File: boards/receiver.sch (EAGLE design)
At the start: 86 parts, among them IC1 7805DT, IC3 XMEGA128a3u, Q1 BC846BSMD, Q2 BC846BSMD, Q3 BC846BSMD, Q4 BC846BSMD, Q5 BC846BSMD, Q6 BC846BSMD, Q7 BC846BSMD, Q8 BC846BSMD

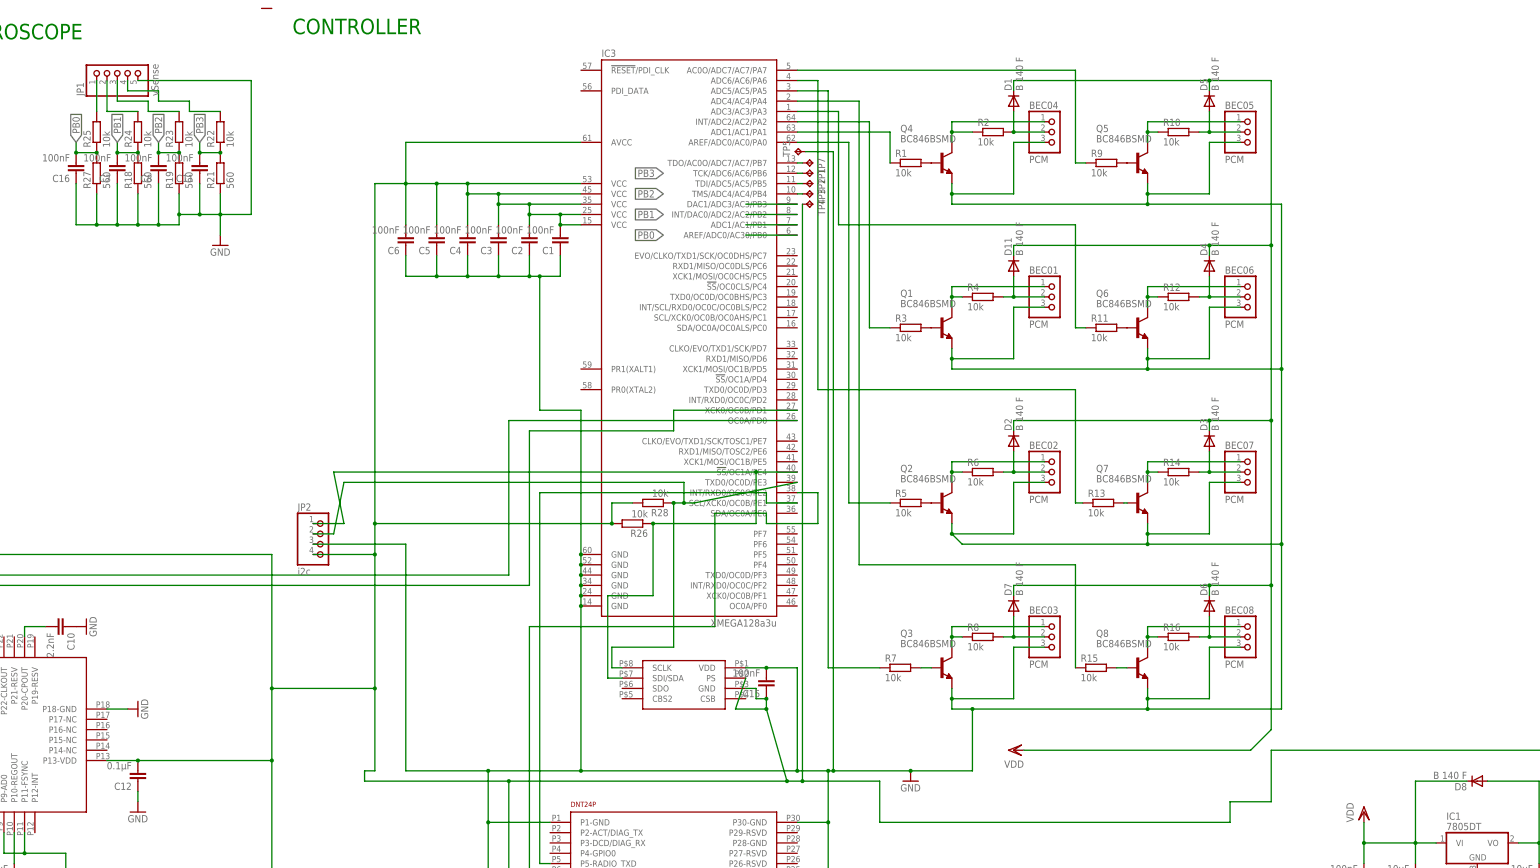
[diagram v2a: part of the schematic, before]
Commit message: Added some status leds
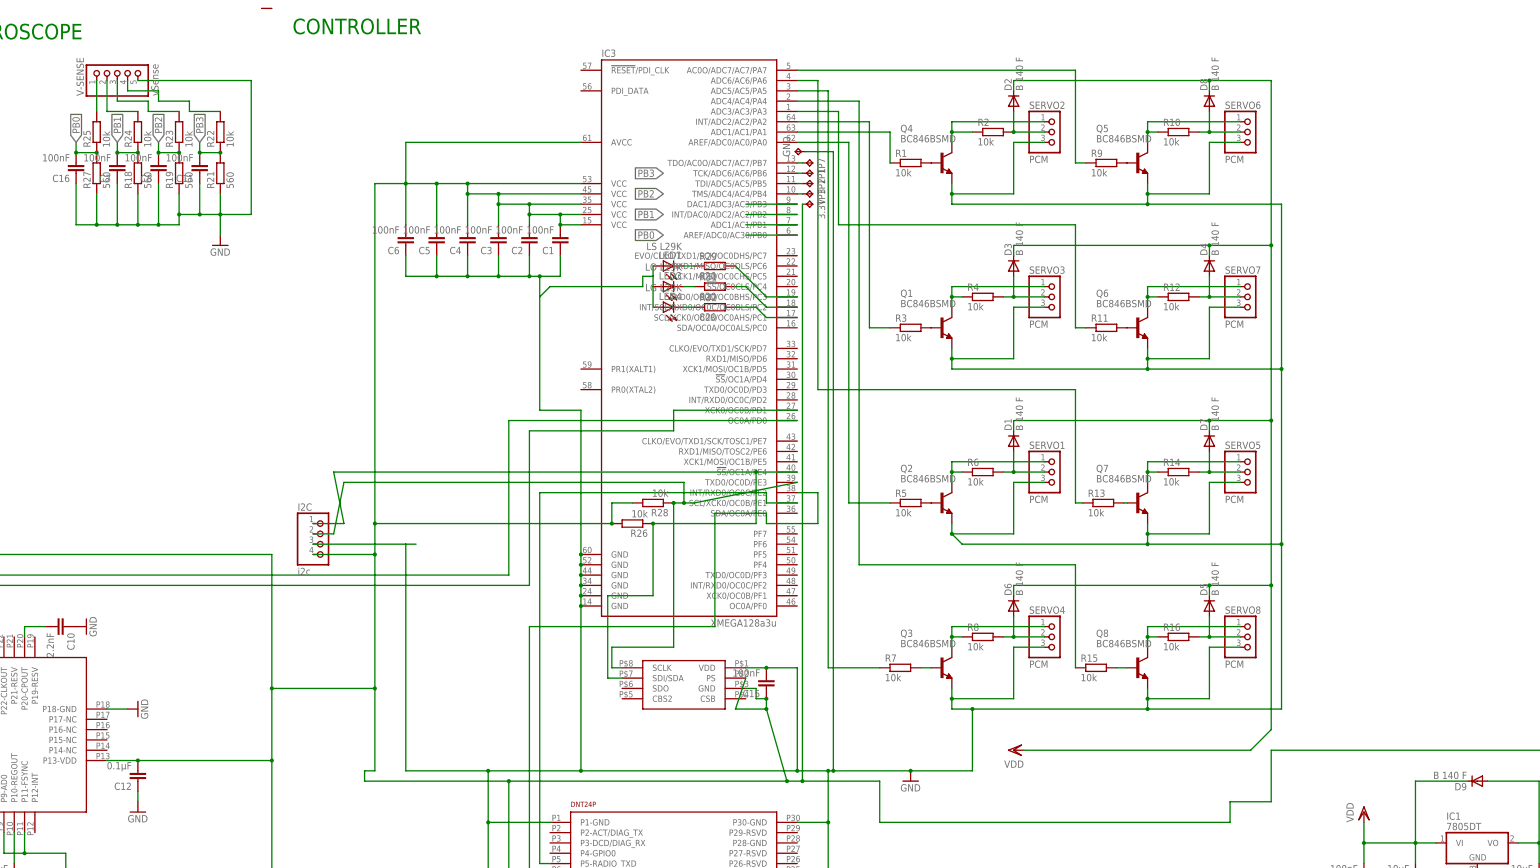
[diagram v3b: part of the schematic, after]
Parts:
- removed D11: B 140 F, diode:CGRM4001-G
- added D9: B 140 F, diode:CGRM4001-G
- added LED1: LS L29K, led:LEDCHIP-LED0603
- added LED3: LO L29K, led:LEDCHIP-LED0603
- added LED4: LG L29K, led:LEDCHIP-LED0603
- added R29, R31, R32: 820, eagle-ltspice:RR0603
- renumbered BEC01 to SERVO3, BEC02 to SERVO1, BEC03 to SERVO4, BEC04 to SERVO2, BEC05 to SERVO6, BEC06 to SERVO7, BEC07 to SERVO5, BEC08 to SERVO8, JP1 to V-SENSE, JP2 to I2C, TP4 to 3.3V, TP5 to GND
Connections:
- new net N$34: LED1.C, R29.1
- new net N$45: IC3.SCL/XCK0/OC0B/OC0AHS/PC1, R32.2
- new net N$48: IC3.INT/SCL/RXD0/OC0C/OC0BLS/PC2, R31.2
- new net N$49: LED3.C, R31.1
- new net N$51: LED4.C, R32.1
- new net N$52: IC3.TXD0/OC0D/OC0BHS/PC3, R29.2
- net GND: now also LED1.A, LED3.A, LED4.A
- net N$12: now also D8.A; no longer D5.A
- net N$15: now also D2.A; no longer D1.A
- net N$20: now also D7.A; no longer D3.A
- net N$23: now also D5.A; no longer D6.A
- net N$3: now also D3.A; no longer D11.A
- net N$6: now also D1.A; no longer D2.A
- net N$9: now also D6.A; no longer D7.A
- net VCC: now also D9.A; no longer D8.A
- net VDD: now also D9.C; no longer D11.C
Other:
- moved on the sheet: D1, D2, D3, D5, D6, D7, D8

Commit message: Added another led, proper resistor values for voltage dividers, layout of silkscreen
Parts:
- added LED2: LS L29K, led:LEDCHIP-LED0603
- added R30: 820, eagle-ltspice:RR0603
- R22, R23, R24, R25: value 10k -> 2.2k
- renumbered SERVO1 to S1, SERVO2 to S2, SERVO3 to S3, SERVO4 to S4, SERVO5 to S5, SERVO6 to S6, SERVO7 to S7, SERVO8 to S8
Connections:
- new net N$53: LED2.C, R30.1
- new net N$54: IC3.!SS!/OC0CLS/PC4, R30.2
- net GND: now also LED2.A
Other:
- moved on the sheet: C17, C18, C19, C21, D9, IC1
